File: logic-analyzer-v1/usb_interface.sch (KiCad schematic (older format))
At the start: 19 parts, among them J1 USB_B_Micro, U1 USBLC6-2SC6_new, U2 FT230XS

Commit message: MOD usb-interface - review and minor fixes
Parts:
- added R6, R7: 27R, Resistor_SMD:R_0603_1608Metric_Pad1.05x0.95mm_HandSolder, symbol Device:R
- FB1: value Ferrite_Bead_Small -> 1k
- U1: symbol Power_Protection_edited:USBLC6-2SC6_new -> logic-analyzer-v1-rescue:USBLC6-2SC6_new-Power_Protection_edited
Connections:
- net labels added: UART_RX, UART_TX, USB_DM, USB_DP
- net labels removed: RXD, TXD
- wire segments 75 -> 72
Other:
- note added: "R3 & R4 - USB for FTDI\nR6 & R7 - USB for MCU"
- moved on the sheet: C1, C2, C3, C4, C5, C6, C7, C8, D1, D2, FB1, R1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

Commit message: modify mcu sheet -> adding front end
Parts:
- renumbered C7 to C?, C6 to C?, C3 to C?, C8 to C?, C2 to C?, C1 to C?, C5 to C?, C4 to C?, D2 to D?, D1 to D?, FB1 to FB?, J1 to J?, R3 to R?, R4 to R?, R2 to R?, R1 to R?, R5 to R?, R6 to R?, R7 to R?, U2 to U?
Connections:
- net labels added: +3V3
- net labels removed: VCC
- wire segments 72 -> 75

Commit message: MOD usb power nets fix, mcu fixes
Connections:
- net labels added: VCC
- net labels removed: +3V3
- wire segments 75 -> 73
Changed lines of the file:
@@
 $EndDescr
-$Comp
-L Device:R R?
-U 1 1 5F09503A
-P 6250 3550
-F 0 "R?" V 6150 3500 50  0000 C CNN
-F 1 "27R" V 6150 3700 50  0000 C CNN
-F 2 "Resistor_SMD:R_0603_1608Metric_Pad1.05x0.95mm_HandSolder" V 6180 3550 50  0001 C CNN
-F 3 "~" H 6250 3550 50  0001 C CNN
-	1    6250 3550
-	0    1    1    0
-$EndComp
-$Comp
-L Device:R R?
-U 1 1 5F095040
-P 6250 3750
-F 0 "R?" V 6150 3700 50  0000 C CNN
-F 1 "27R" V 6150 3900 50  0000 C CNN
-F 2 "Resistor_SMD:R_0603_1608Metric_Pad1.05x0.95mm_HandSolder" V 6180 3750 50  0001 C CNN
-F 3 "~" H 6250 3750 50  0001 C CNN
-	1    6250 3750
-	0    1    1    0
-$EndComp
 $Comp
 L Device:C C?
@@
 	1    0    0    -1
 $EndComp
-$Comp
-L Device:R R?
-U 1 1 5F0E9124
-P 6250 4300
-F 0 "R?" V 6150 4250 50  0000 C CNN
-F 1 "27R" V 6150 4450 50  0000 C CNN
-F 2 "Resistor_SMD:R_0603_1608Metric_Pad1.05x0.95mm_HandSolder" V 6180 4300 50  0001 C CNN
-F 3 "~" H 6250 4300 50  0001 C CNN
-	1    6250 4300
-	0    1    1    0
-$EndComp
-$Comp
-L Device:R R?
-U 1 1 5F0E9480
-P 6250 4500
-F 0 "R?" V 6150 4450 50  0000 C CNN
-F 1 "27R" V 6150 4650 50  0000 C CNN
-F 2 "Resistor_SMD:R_0603_1608Metric_Pad1.05x0.95mm_HandSolder" V 6180 4500 50  0001 C CNN
-F 3 "~" H 6250 4500 50  0001 C CNN
-	1    6250 4500
-	0    1    1    0
-$EndComp
-Wire Wire Line
-	5900 3550 5100 3550
 Wire Wire Line
 	5850 4500 6100 4500
@@
 R3 & R4 - USB for FTDI\nR6 & R7 - USB for MCU
 Wire Wire Line
-	5900 3550 6100 3550
-Wire Wire Line
-	5900 3550 5900 4300
-Wire Wire Line
-	6400 3550 7350 3550
-Wire Wire Line
 	7350 3550 7350 3650
-Connection ~ 5900 3550
 Wire Wire Line
 	5850 3750 5850 4500
@@
 Wire Wire Line
 	6400 4300 6750 4300
-Wire Notes Line
-	6000 3350 6550 3350
-Wire Notes Line
-	6550 3350 6550 4750
-Wire Notes Line
-	6550 4750 7150 4750
 Wire Notes Line
 	7150 4750 7150 5100
@@
 Wire Wire Line
 	3450 4700 3450 4950
-Text HLabel 9900 4350 2    50   UnSpc ~ 10
-+3V3
-Wire Wire Line
-	9900 4350 9750 4350
-Wire Wire Line
-	9750 4350 9750 4300
-$Comp
-L power:+3V3 #PWR?
-U 1 1 5F52835A
-P 9750 4300
-AR Path="/5F19654C/5F52835A" Ref="#PWR?"  Part="1"
-AR Path="/5F08ED8D/5F52835A" Ref="#PWR?"  Part="1"
-F 0 "#PWR?" H 9750 4150 50  0001 C CNN
-F 1 "+3V3" H 9765 4473 50  0000 C CNN
-F 2 "" H 9750 4300 50  0001 C CNN
-F 3 "" H 9750 4300 50  0001 C CNN
-	1    9750 4300
-	1    0    0    -1
-$EndComp
-$Comp
-L power:+3V3 #PWR?
-U 1 1 5F52ACF7
-P 7950 2650
-AR Path="/5F19654C/5F52ACF7" Ref="#PWR?"  Part="1"
-AR Path="/5F08ED8D/5F52ACF7" Ref="#PWR?"  Part="1"
-F 0 "#PWR?" H 7950 2500 50  0001 C CNN
-F 1 "+3V3" H 7965 2823 50  0000 C CNN
-F 2 "" H 7950 2650 50  0001 C CNN
-F 3 "" H 7950 2650 50  0001 C CNN
-	1    7950 2650
-	1    0    0    -1
-$EndComp
-$Comp
-L power:+3V3 #PWR?
-U 1 1 5F52B33B
-P 4950 2650
-AR Path="/5F19654C/5F52B33B" Ref="#PWR?"  Part="1"
-AR Path="/5F08ED8D/5F52B33B" Ref="#PWR?"  Part="1"
-F 0 "#PWR?" H 4950 2500 50  0001 C CNN
-F 1 "+3V3" H 4965 2823 50  0000 C CNN
-F 2 "" H 4950 2650 50  0001 C CNN
-F 3 "" H 4950 2650 50  0001 C CNN
-	1    4950 2650
-	1    0    0    -1
-$EndComp
-$Comp
-L power:+3V3 #PWR?
+$Comp
+L power:VCC #PWR?
 U 1 1 5F52B97E
 P 3600 2650
@@
 AR Path="/5F08ED8D/5F52B97E" Ref="#PWR?"  Part="1"
 F 0 "#PWR?" H 3600 2500 50  0001 C CNN
-F 1 "+3V3" H 3615 2823 50  0000 C CNN
+F 1 "VCC" H 3615 2823 50  0000 C CNN
 F 2 "" H 3600 2650 50  0001 C CNN
 F 3 "" H 3600 2650 50  0001 C CNN
@@
 	1    0    0    -1
 $EndComp
-$Comp
-L power:+3V3 #PWR?
-U 1 1 5F52BDA1
+Wire Wire Line
+	3600 2650 3600 2950
+$Comp
+L power:VCC #PWR?
+U 1 1 5F414476
+P 4950 2650
+AR Path="/5F19654C/5F414476" Ref="#PWR?"  Part="1"
+AR Path="/5F08ED8D/5F414476" Ref="#PWR?"  Part="1"
+F 0 "#PWR?" H 4950 2500 50  0001 C CNN
+F 1 "VCC" H 4965 2823 50  0000 C CNN
+F 2 "" H 4950 2650 50  0001 C CNN
+F 3 "" H 4950 2650 50  0001 C CNN
+	1    4950 2650
+	1    0    0    -1
+$EndComp
+Wire Wire Line
+	4950 2650 4950 3350
+$Comp
+L power:VCC #PWR?
+U 1 1 5F415F7E
+P 7950 2650
+AR Path="/5F19654C/5F415F7E" Ref="#PWR?"  Part="1"
+AR Path="/5F08ED8D/5F415F7E" Ref="#PWR?"  Part="1"
+F 0 "#PWR?" H 7950 2500 50  0001 C CNN
+F 1 "VCC" H 7965 2823 50  0000 C CNN
+F 2 "" H 7950 2650 50  0001 C CNN
+F 3 "" H 7950 2650 50  0001 C CNN
+	1    7950 2650
+	1    0    0    -1
+$EndComp
+$Comp
+L power:VCC #PWR?
+U 1 1 5F4189D9
 P 3450 4700
-AR Path="/5F19654C/5F52BDA1" Ref="#PWR?"  Part="1"
-AR Path="/5F08ED8D/5F52BDA1" Ref="#PWR?"  Part="1"
+AR Path="/5F19654C/5F4189D9" Ref="#PWR?"  Part="1"
+AR Path="/5F08ED8D/5F4189D9" Ref="#PWR?"  Part="1"
 F 0 "#PWR?" H 3450 4550 50  0001 C CNN
-F 1 "+3V3" H 3465 4873 50  0000 C CNN
+F 1 "VCC" H 3465 4873 50  0000 C CNN
 F 2 "" H 3450 4700 50  0001 C CNN
 F 3 "" H 3450 4700 50  0001 C CNN
@@
 	1    0    0    -1
 $EndComp
-Wire Wire Line
-	4950 2650 4950 3350
-Wire Wire Line
-	3600 2650 3600 2950
+Connection ~ 5900 3550
+Wire Wire Line
+	5900 3550 5900 4300
+Wire Wire Line
+	5900 3550 5100 3550
+Wire Wire Line
+	5900 3550 6100 3550
+Wire Wire Line
+	6400 3550 7350 3550
+$Comp
+L Device:R R?
+U 1 1 5F0E9480
+P 6250 4500
+F 0 "R?" V 6150 4450 50  0000 C CNN
+F 1 "27R" V 6150 4650 50  0000 C CNN
+F 2 "Resistor_SMD:R_0603_1608Metric_Pad1.05x0.95mm_HandSolder" V 6180 4500 50  0001 C CNN
+F 3 "~" H 6250 4500 50  0001 C CNN
+	1    6250 4500
+	0    1    1    0
+$EndComp
+$Comp
+L Device:R R?
+U 1 1 5F0E9124
+P 6250 4300
+F 0 "R?" V 6150 4250 50  0000 C CNN
+F 1 "27R" V 6150 4450 50  0000 C CNN
+F 2 "Resistor_SMD:R_0603_1608Metric_Pad1.05x0.95mm_HandSolder" V 6180 4300 50  0001 C CNN
+F 3 "~" H 6250 4300 50  0001 C CNN
+	1    6250 4300
+	0    1    1    0
+$EndComp
+$Comp
+L Device:R R?
+U 1 1 5F095040
+P 6250 3750
+F 0 "R?" V 6150 3700 50  0000 C CNN
+F 1 "27R" V 6150 3900 50  0000 C CNN
+F 2 "Resistor_SMD:R_0603_1608Metric_Pad1.05x0.95mm_HandSolder" V 6180 3750 50  0001 C CNN
+F 3 "~" H 6250 3750 50  0001 C CNN
+	1    6250 3750
+	0    1    1    0
+$EndComp
+$Comp
+L Device:R R?
+U 1 1 5F09503A
+P 6250 3550
+F 0 "R?" V 6150 3500 50  0000 C CNN
+F 1 "27R" V 6150 3700 50  0000 C CNN
+F 2 "Resistor_SMD:R_0603_1608Metric_Pad1.05x0.95mm_HandSolder" V 6180 3550 50  0001 C CNN
+F 3 "~" H 6250 3550 50  0001 C CNN
+	1    6250 3550
+	0    1    1    0
+$EndComp
+Wire Notes Line
+	6000 3350 6550 3350
+Wire Notes Line
+	6550 4750 7150 4750
+Wire Notes Line
+	6550 3350 6550 4750
 $EndSCHEMATC

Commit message: adding gpio pins, usb pins, usart pins
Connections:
- net labels added: USB_DN
- net labels removed: USB_DM
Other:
- moved on the sheet: C?
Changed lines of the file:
@@
 L Device:C C?
 U 1 1 5F09508A
-P 3650 5100
-F 0 "C?" H 3765 5146 50  0000 L CNN
-F 1 "4.7u" H 3765 5055 50  0000 L CNN
-F 2 "Capacitor_SMD:C_1206_3216Metric_Pad1.42x1.75mm_HandSolder" H 3688 4950 50  0001 C CNN
-F 3 "https://www.tme.eu/pl/details/c1206c475k3racauto/kondensatory-mlcc-smd-1206/kemet/" H 3650 5100 50  0001 C CNN
-F 4 "https://www.tme.eu/pl/details/c1206c475k3racauto/kondensatory-mlcc-smd-1206/kemet/" H 3650 5100 50  0001 C CNN "link"
-	1    3650 5100
+P 3600 5050
+F 0 "C?" H 3715 5096 50  0000 L CNN
+F 1 "4.7u" H 3715 5005 50  0000 L CNN
+F 2 "Capacitor_SMD:C_1206_3216Metric_Pad1.42x1.75mm_HandSolder" H 3638 4900 50  0001 C CNN
+F 3 "https://www.tme.eu/pl/details/c1206c475k3racauto/kondensatory-mlcc-smd-1206/kemet/" H 3600 5050 50  0001 C CNN
+F 4 "https://www.tme.eu/pl/details/c1206c475k3racauto/kondensatory-mlcc-smd-1206/kemet/" H 3600 5050 50  0001 C CNN "link"
+	1    3600 5050
 	1    0    0    -1
 $EndComp
@@
 L Device:C C?
 U 1 1 5F0950BF
-P 3250 5100
-F 0 "C?" H 3365 5146 50  0000 L CNN
-F 1 "100n" H 3365 5055 50  0000 L CNN
-F 2 "Capacitor_SMD:C_0603_1608Metric_Pad1.05x0.95mm_HandSolder" H 3288 4950 50  0001 C CNN
-F 3 "~" H 3250 5100 50  0001 C CNN
-	1    3250 5100
+P 3200 5050
+F 0 "C?" H 3315 5096 50  0000 L CNN
+F 1 "100n" H 3315 5005 50  0000 L CNN
+F 2 "Capacitor_SMD:C_0603_1608Metric_Pad1.05x0.95mm_HandSolder" H 3238 4900 50  0001 C CNN
+F 3 "~" H 3200 5050 50  0001 C CNN
+	1    3200 5050
 	1    0    0    -1
 $EndComp
@@
 L power:GND #PWR?
 U 1 1 5F0950C5
-P 3450 5450
-F 0 "#PWR?" H 3450 5200 50  0001 C CNN
-F 1 "GND" H 3455 5277 50  0000 C CNN
-F 2 "" H 3450 5450 50  0001 C CNN
-F 3 "" H 3450 5450 50  0001 C CNN
-	1    3450 5450
-	1    0    0    -1
-$EndComp
-Wire Wire Line
-	3250 4950 3450 4950
-Wire Wire Line
-	3650 4950 3450 4950
-Connection ~ 3450 4950
-Wire Wire Line
-	3250 5250 3450 5250
-Wire Wire Line
-	3450 5250 3450 5450
-Wire Wire Line
-	3450 5250 3650 5250
-Connection ~ 3450 5250
+P 3400 5400
+F 0 "#PWR?" H 3400 5150 50  0001 C CNN
+F 1 "GND" H 3405 5227 50  0000 C CNN
+F 2 "" H 3400 5400 50  0001 C CNN
+F 3 "" H 3400 5400 50  0001 C CNN
+	1    3400 5400
+	1    0    0    -1
+$EndComp
+Wire Wire Line
+	3200 4900 3400 4900
+Wire Wire Line
+	3600 4900 3400 4900
+Connection ~ 3400 4900
+Wire Wire Line
+	3200 5200 3400 5200
+Wire Wire Line
+	3400 5200 3400 5400
+Wire Wire Line
+	3400 5200 3600 5200
+Connection ~ 3400 5200
 $Comp
 L Device:C C?
@@
 USB_DP
 Text HLabel 6750 4300 2    50   BiDi ~ 0
-USB_DM
+USB_DN
 Wire Wire Line
 	6400 4500 6750 4500
@@
 Connection ~ 7950 2750
 Wire Wire Line
-	3450 4700 3450 4950
+	3400 4650 3400 4900
 $Comp
 L power:VCC #PWR?
@@
 L power:VCC #PWR?
 U 1 1 5F4189D9
-P 3450 4700
+P 3400 4650
 AR Path="/5F19654C/5F4189D9" Ref="#PWR?"  Part="1"
 AR Path="/5F08ED8D/5F4189D9" Ref="#PWR?"  Part="1"
-F 0 "#PWR?" H 3450 4550 50  0001 C CNN
-F 1 "VCC" H 3465 4873 50  0000 C CNN
-F 2 "" H 3450 4700 50  0001 C CNN
-F 3 "" H 3450 4700 50  0001 C CNN
-	1    3450 4700
-	1    0    0    -1
-$EndComp
+F 0 "#PWR?" H 3400 4500 50  0001 C CNN
+F 1 "VCC" H 3415 4823 50  0000 C CNN
+F 2 "" H 3400 4650 50  0001 C CNN
+F 3 "" H 3400 4650 50  0001 C CNN
+	1    3400 4650
+	1    0    0    -1
+$EndComp

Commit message: update 03.2021
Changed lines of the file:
@@
 $Descr A4 11693 8268
 encoding utf-8
-Sheet 2 3
+Sheet 2 6
 Title ""
 Date ""
@@
 Connection ~ 8150 3000
 Connection ~ 7200 3350
-Text HLabel 6750 4500 2    50   BiDi ~ 0
+Text HLabel 6650 4500 2    50   BiDi ~ 0
 USB_DP
-Text HLabel 6750 4300 2    50   BiDi ~ 0
+Text HLabel 6650 4300 2    50   BiDi ~ 0
 USB_DN
 Wire Wire Line
-	6400 4500 6750 4500
-Wire Wire Line
-	6400 4300 6750 4300
+	6400 4500 6650 4500
+Wire Wire Line
+	6400 4300 6650 4300
 Wire Notes Line
 	7150 4750 7150 5100

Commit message: add comparator&sram
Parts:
- J?: symbol Connector:USB_B_Micro -> logic-analyzer-v1-rescue:USB_B_Micro-Connector
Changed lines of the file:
@@
 $EndComp
 $Comp
-L Connector:USB_B_Micro J?
+L logic-analyzer-v1-rescue:USB_B_Micro-Connector J?
 U 1 1 5F095083
 P 2700 3150

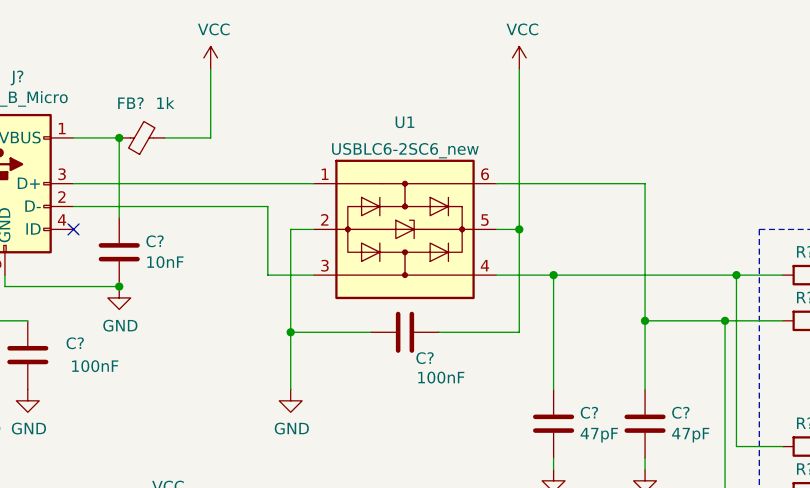
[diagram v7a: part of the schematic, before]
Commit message: improvement origin in libraries and creation my_library containing all ours libraries
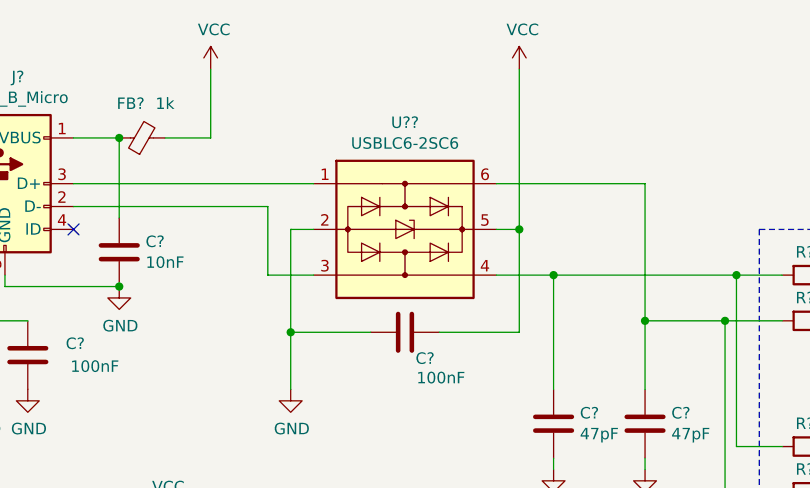
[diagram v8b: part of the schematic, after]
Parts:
- removed U1: USBLC6-2SC6_new, Package_TO_SOT_SMD:SOT-23-6, symbol logic-analyzer-v1-rescue:USBLC6-2SC6_new-Power_Protection_edited
- added U??: USBLC6-2SC6, Package_TO_SOT_SMD:SOT-23-6, symbol my_library:USBLC6-2SC6
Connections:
- net GND: now also U??.2 (GND)
- net VCC: now also U??.5 (VBUS)
- net at C?.1, R?.2, R?.2: now also U??.4 (I/O2)
- net at C?.1, R?.2, R?.2: now also U??.6 (I/O1)
- net at J?.2 (D-): now also U??.3 (I/O2)
- net at J?.3 (D+): now also U??.1 (I/O1)
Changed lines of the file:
@@
 	0    -1   -1   0
-$EndComp
-$Comp
-L logic-analyzer-v1-rescue:USBLC6-2SC6_new-Power_Protection_edited U?
-U 1 1 5F09511D
-P 4450 3350
-AR Path="/5F09511D" Ref="U?"  Part="1"
-AR Path="/5F08ED8D/5F09511D" Ref="U1"  Part="1"
-F 0 "U1" V 3983 3350 50  0000 C CNN
-F 1 "USBLC6-2SC6_new" V 4100 3350 50  0000 C CNN
-F 2 "Package_TO_SOT_SMD:SOT-23-6" H 5300 3700 50  0001 C CNN
-F 3 "https://www.st.com/resource/en/datasheet/usblc6-2.pdf" H 4650 3700 50  0001 C CNN
-	1    4450 3350
-	0    1    1    0
 $EndComp
 Wire Wire Line
@@
 Wire Notes Line
 	6550 3350 6550 4750
+$Comp
+L my_library:USBLC6-2SC6 U??
+U 1 1 6087567F
+P 4450 3350
+F 0 "U??" H 4450 3817 50  0000 C CNN
+F 1 "USBLC6-2SC6" H 4450 3726 50  0000 C CNN
+F 2 "Package_TO_SOT_SMD:SOT-23-6" H 4500 2900 50  0001 C CNN
+F 3 "" V 4800 3150 50  0001 C CNN
+	1    4450 3350
+	1    0    0    -1
+$EndComp
 $EndSCHEMATC
